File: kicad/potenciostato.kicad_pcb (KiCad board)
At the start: 2 copper layers, 150 x 100 mm, 51 parts, among them J1 Conn_01x03_Female, J2 USB_B_Micro, J3 Conn_01x03_Male, U1 OP77, U2 TL082, U3 OP77, U4 OP77, U5 4016, U6 4016, U7 TL064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

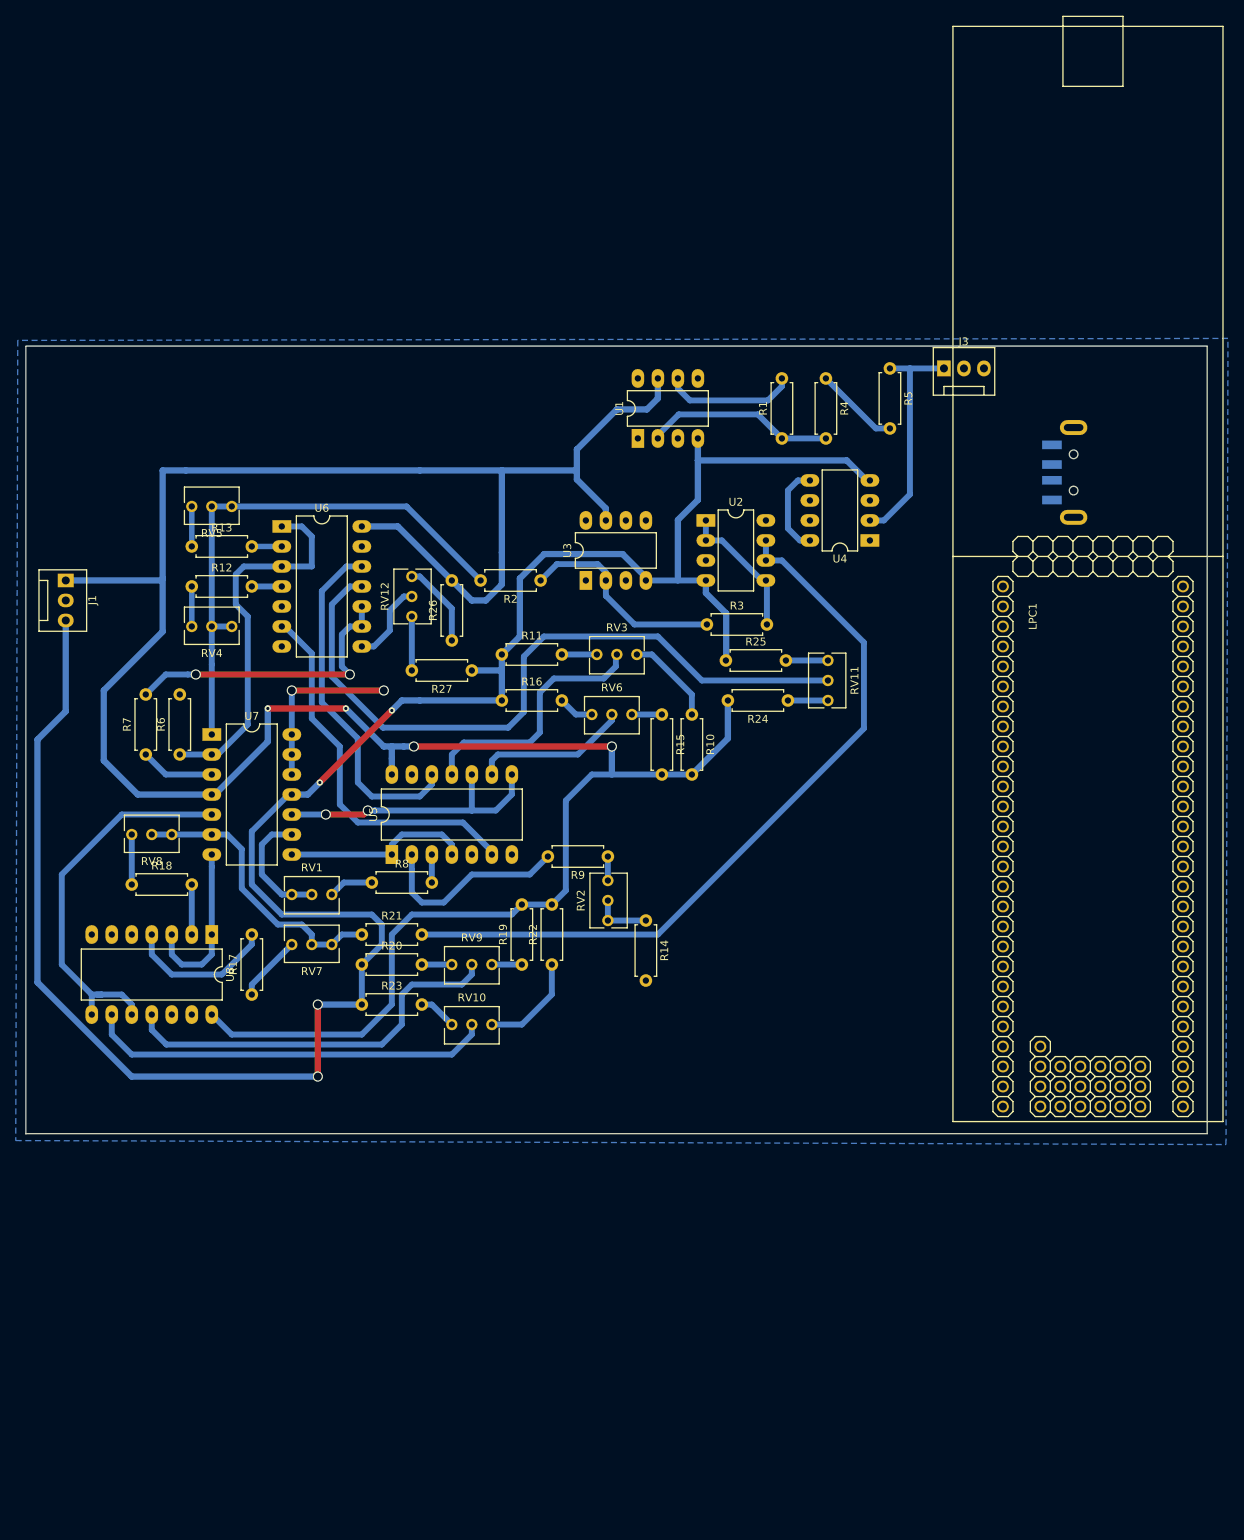
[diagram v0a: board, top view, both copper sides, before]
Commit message: ruteado LPC, falta pines
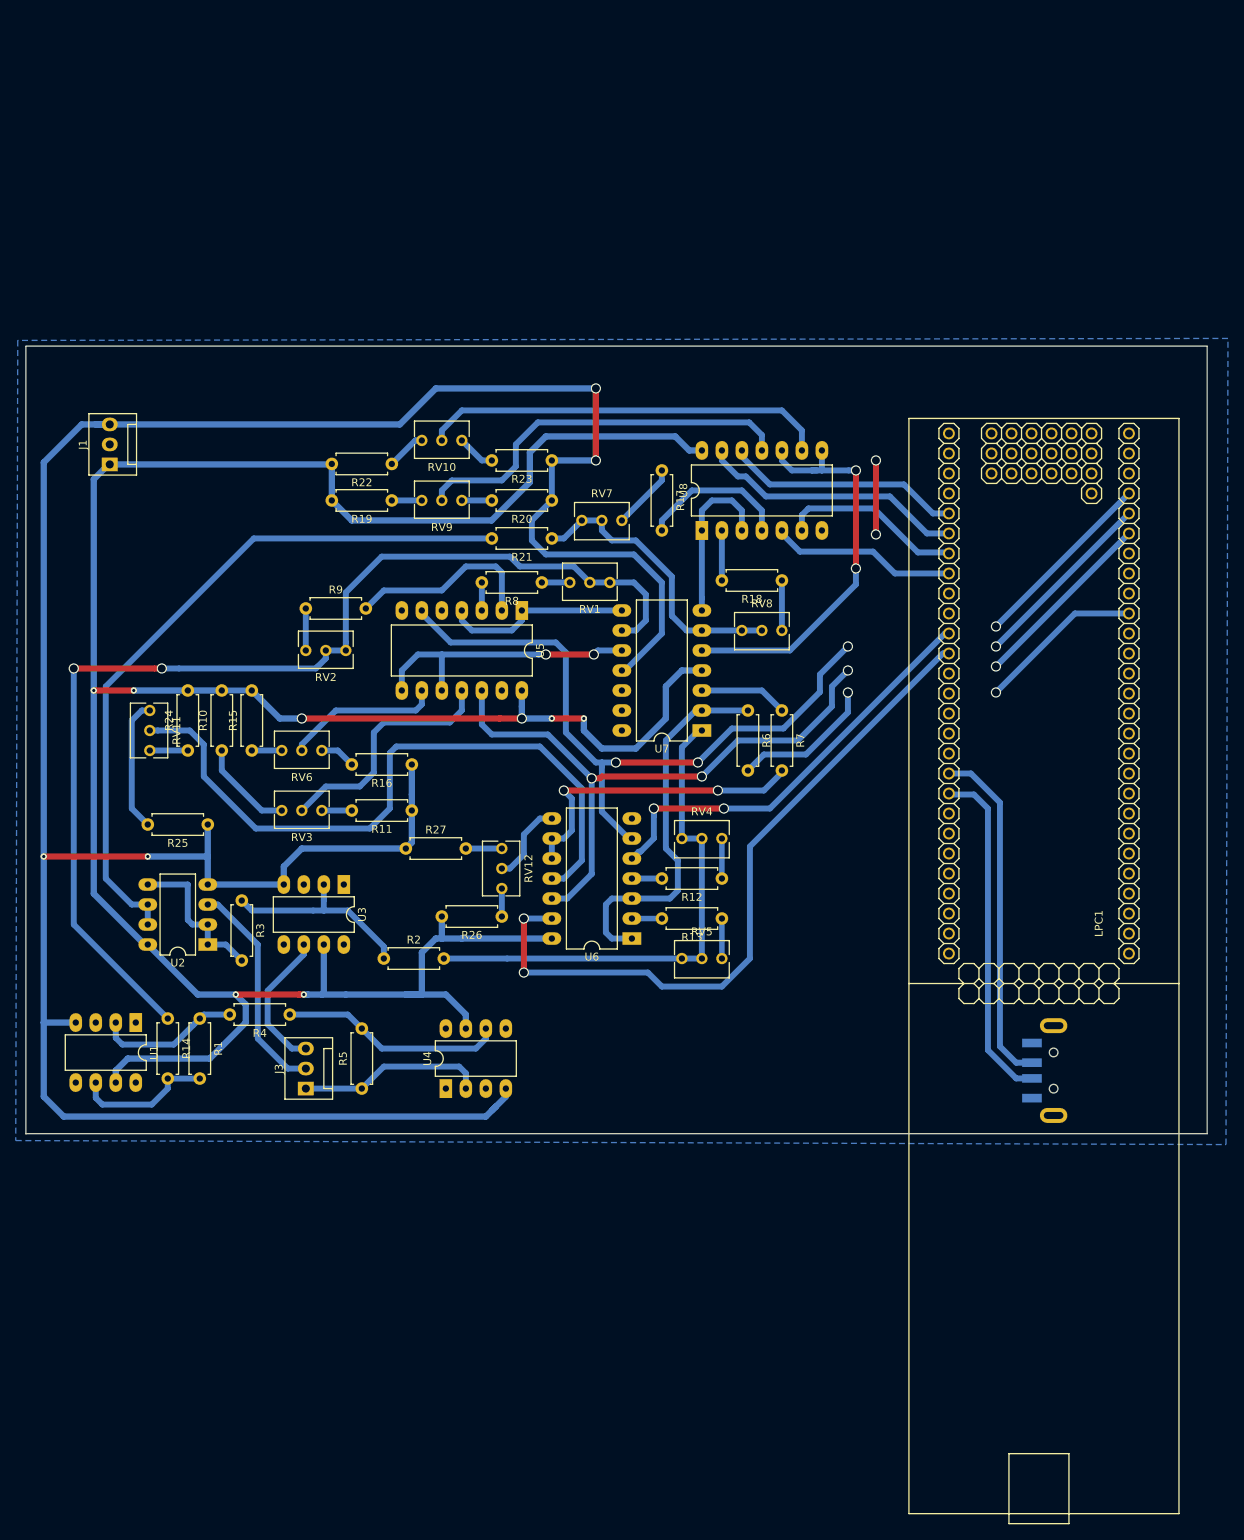
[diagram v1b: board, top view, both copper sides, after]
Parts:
- moved J3 122.2 mm to (685.5, 96.8), turned to 90 degrees
- moved LPC1 114.0 mm to (784.4, 113.3), turned to 90 degrees
- moved R5 113.4 mm to (692.7, 96.8), turned to 90 degrees
- moved R4 105.6 mm to (683.5, 87.4), turned to 180 degrees
- moved R1 104.4 mm to (672.1, 87.9), turned to 270 degrees
- moved U1 97.8 mm to (664.0, 88.4), turned to 270 degrees
- moved R18 91.1 mm to (746.0, 32.3), turned to 180 degrees
- moved RV5 88.5 mm to (738.4, 80.3), turned to 0 degrees
- moved U4 88.0 mm to (703.3, 96.8), turned to 90 degrees
- moved RV8 86.5 mm to (746.0, 38.6), turned to 0 degrees
- moved RV11 86.3 mm to (665.7, 53.8)
- moved R17 84.5 mm to (730.8, 18.3), turned to 270 degrees
- moved U2 83.1 mm to (673.1, 78.5), turned to 180 degrees
- moved R13 82.2 mm to (738.4, 75.2), turned to 180 degrees
- moved R7 81.0 mm to (746.0, 48.8), turned to 270 degrees
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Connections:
- J2 pad 5: Net-(J2-Pad5) -> GND
- LPC1 pad 43: /LPC/P2.1 -> /LPC/P2.2
- LPC1 pad 44: /LPC/P2.2 -> /LPC/P2.1
- LPC1 pad 48: /LPC/P2.6 -> /salida_dac/OFF_V_1
- LPC1 pad 49: /salida_dac/OFF_V_1 -> /LPC/P2.6
- LPC1 pad 54: Net-(J2-Pad5) -> GND
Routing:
- net Net-(R14-Pad1): track 22.9 -> 141.7 mm, vias 0 -> 2
- net /LPC/P2.2: track 0.00 -> 91.0 mm, vias 0 -> 2
- net -5V: track 278.1 -> 349.5 mm
- net /salida_dac/OFF_I_1: track 48.1 -> 111.0 mm, vias 0 -> 4
- net /salida_dac/OFF_I_2: track 44.6 -> 103.2 mm, vias 0 -> 4
- net /LPC/P2.1: track 0.00 -> 54.3 mm, vias 0 -> 2
- net Net-(J2-Pad3): track 0.00 -> 43.9 mm
- net Net-(J2-Pad2): track 0.00 -> 43.5 mm
- net /LPC/DAC: track 0.00 -> 39.3 mm, vias 0 -> 2
- net /LPC/P2.6: track 0.00 -> 33.9 mm
- net /salida_dac/OFF_V_2: track 0.00 -> 30.0 mm
- net Net-(J3-Pad2): track 0.18 -> 28.2 mm
- net /LPC/P0.3: track 0.00 -> 23.9 mm, vias 0 -> 1
- net /LPC/P2.5: track 0.00 -> 23.9 mm
- net /salida_dac/OFF_V_1: track 0.00 -> 23.3 mm
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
